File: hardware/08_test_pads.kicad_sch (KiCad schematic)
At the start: 63 parts

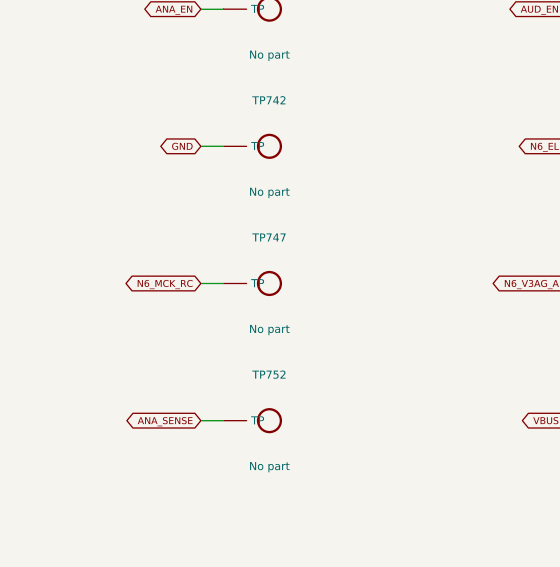
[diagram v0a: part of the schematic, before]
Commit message: fix: close the independent layout review v1.0 (T1-T7, D1-D3); verified on the reviewer's solvers
Layout (blocks b25-b33, replayed by the generator):
- T1 MCLK-alive detector: C625/R666/R667 in a row at D609; hold node 3.4 mm, no vias (was 68 mm,
  8 vias). The old trunk becomes the DC side N6_MCK_CMP. TP747 behind R667 (ECO F13).
- T2 ECO F11: R247-R249, 33 ohm, at the U208 LINK outputs; R249 returns on In3; C224 above U208.
- T3 ECO F12: R203 33 ohm -> 0 ohm (BOM only).
- T4 six filled 0.7/0.3 vias in the U503 PowerPAD; 3V3M/ANA_EN/AUD_EN/N5_ILIM detours.
- T5 C217/C218/C219 at the X201-X203 VCC pins (X203 shifted 1 mm, R218 relocated).
- T6 C206/C207 to U201 pins 64/32 (pins 1/19: no legal site).
- EP vias U504 +2, U401 +3, U402 +4; J701 sleeve 2 -> 5 GND vias; R1 board corner fixed.

Generator: schematic sync (fields, DNP, NC-pin nets) gives 0 parity issues (T7, D3); ECO footprint
copies get fresh UUIDs; value overrides. New CI step check_integrated_parity.py (DRC + parity).

Re-verified with the reviewer's evidence code on the new board (sim/layout_review_v1):
detector dead-worst 0.481 -> 0.458 ms; LINK_SCK clamp 14.3 -> 0 mA; U503 fault 131.3 -> 117.9 C;
oscillator spikes 175-189 -> 60-69 mV; MCU droop pins 32/64 102-103 -> 41/30 mV.

Docs: LAYOUT_REVIEW_RESPONSE_2026-10-13.md, DESIGN_DOCUMENT_UPDATES_2026-10-13.md (Parts List
v1.0 and Spec/Notes change lists for the owner), DESIGN_TO_LAYOUT_DIFFERENCES.md, 1:1 print for T8.

Co-Authored-By: Claude Opus 5.5 <noreply@anthropic.com>
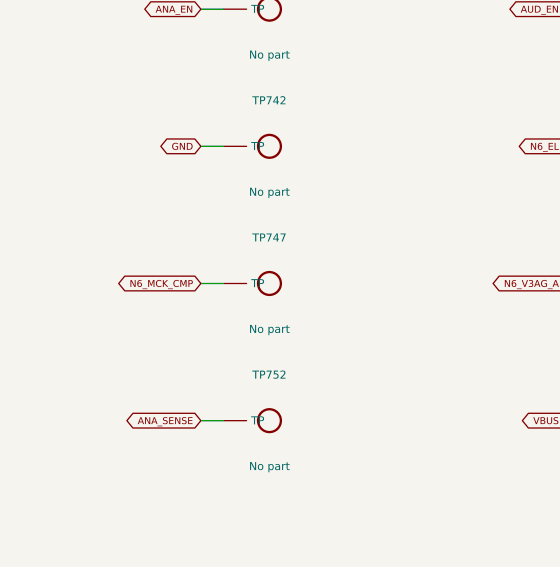
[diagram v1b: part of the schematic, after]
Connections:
- net N6_MCK_RC renamed N6_MCK_CMP
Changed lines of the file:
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@@
 )
 (wire (pts (xy 43.18 198.12) (xy 40.64 198.12)) (stroke (width 0) (type solid)))
-(global_label "N6_MCK_RC" (shape bidirectional) (at 40.64 198.12 180) (effects (font (size 0.762 0.762)) (justify right bottom)))
+(global_label "N6_MCK_CMP" (shape bidirectional) (at 40.64 198.12 180) (effects (font (size 0.762 0.762)) (justify right bottom)))
 (symbol (lib_id "DAC_HPA:P183") (at 88.9 198.12 0) (unit 1) (exclude_from_sim no) (in_bom no) (on_board yes) (dnp no)
 (property "Reference" "TP748" (at 88.9 193.04 0) (effects (font (size 0.889 0.889))))
